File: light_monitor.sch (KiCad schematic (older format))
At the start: 28 parts, among them IC1 TSL237S-LF, J1 Conn_01x03, J2 Conn_01x04_Male, U1 STM32L432KCUx, U2 STDC14, U3 TG-3541CE, U4 sm_tsl237, U5 REG710-3, U6 LT1677CS8

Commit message: rev 10 board
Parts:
- removed H2: MountingHole, MountingHole:MountingHole_2.2mm_M2_Pad_Via, symbol Mechanical:MountingHole
- removed U4: sm_tsl237, bhimebau_lightsensor:tsl237t, symbol bhimebau_lightsensor:sm_tsl237
- removed U5: REG710-3, Package_TO_SOT_SMD:SOT-23-6_Handsoldering, symbol bhimebau-switch-mode-supply:REG710-3
- removed U6: LT1677CS8, ltc1677:SO-8_S, symbol ltc1677:LT1677CS8
- added C4, C6, C7: 0.1uF, Capacitor_SMD:C_0603_1608Metric_Pad1.05x0.95mm_HandSolder, symbol Device:C
- added C5: 1uF, Capacitor_SMD:C_0603_1608Metric_Pad1.05x0.95mm_HandSolder, symbol Device:C
- added R1, R10, R11, R12, R9: R_US, Resistor_SMD:R_0603_1608Metric_Pad1.05x0.95mm_HandSolder, symbol Device:R_US
- added TP1, TP10, TP11, TP2, TP3, TP4, TP5, TP6, TP7, TP8, TP9: TestPoint, TestPoint:TestPoint_Pad_D1.5mm, symbol Connector:TestPoint
- added U4: TPS7A05, Package_TO_SOT_SMD:SOT-23, symbol bhimebau_regulator:TPS7A05
- added U5: TPS22917, Package_TO_SOT_SMD:SOT-23-6_Handsoldering, symbol bhimebau_switch:TPS22917
- added U6: AD8515, Package_TO_SOT_SMD:SOT-353_SC-70-5_Handsoldering, symbol bhimebau_opamp:AD8515
- BT1: footprint bhimebau_battery:BR2330A_Horizontal_Circular_Holes -> bhimebau_battery:TLH-5935
- C1, C2: value 2.2uF -> 1uF
- C3: value 0.1uF -> 1uF
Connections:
- net labels added: +BATT, +VSW, CLKOUT, batt_measure, sensor_pwr
- net labels removed: current_feedback, sensor_3v, tsl237_pwr
- wire segments 100 -> 145
- no-connect marks 23 -> 18
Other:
- note added: "VDD = 2V"
- moved on the sheet: BT1, C11, D2, H1, H3, H4, IC1, R2

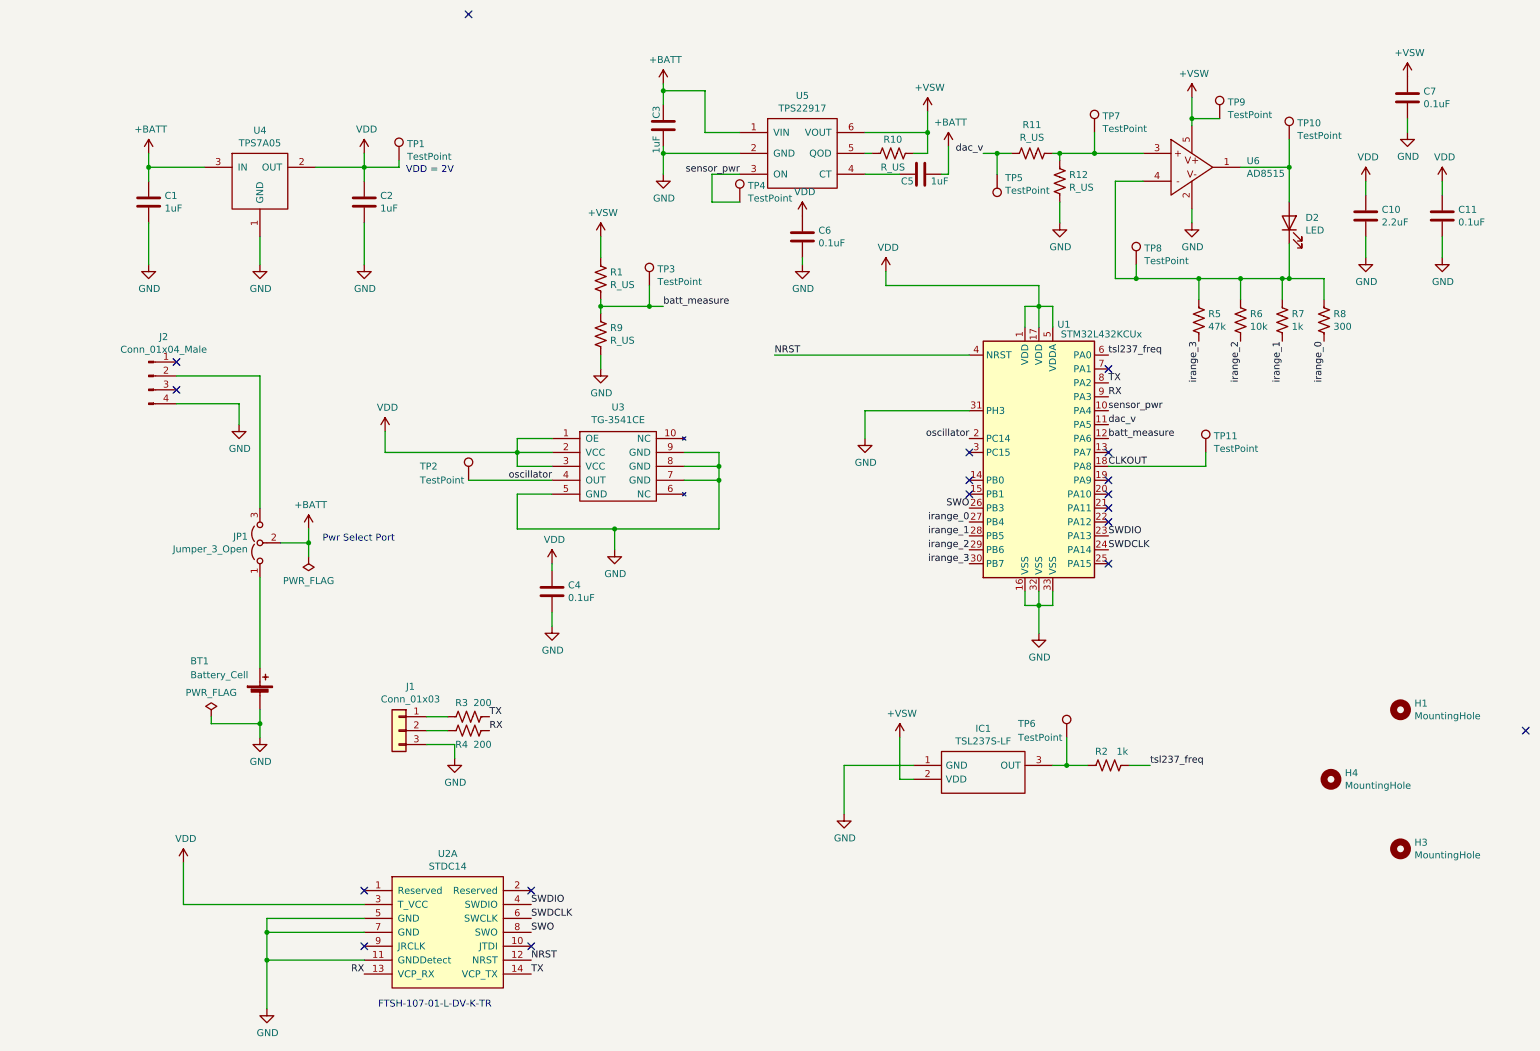
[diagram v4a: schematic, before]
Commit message: added the version used by the students
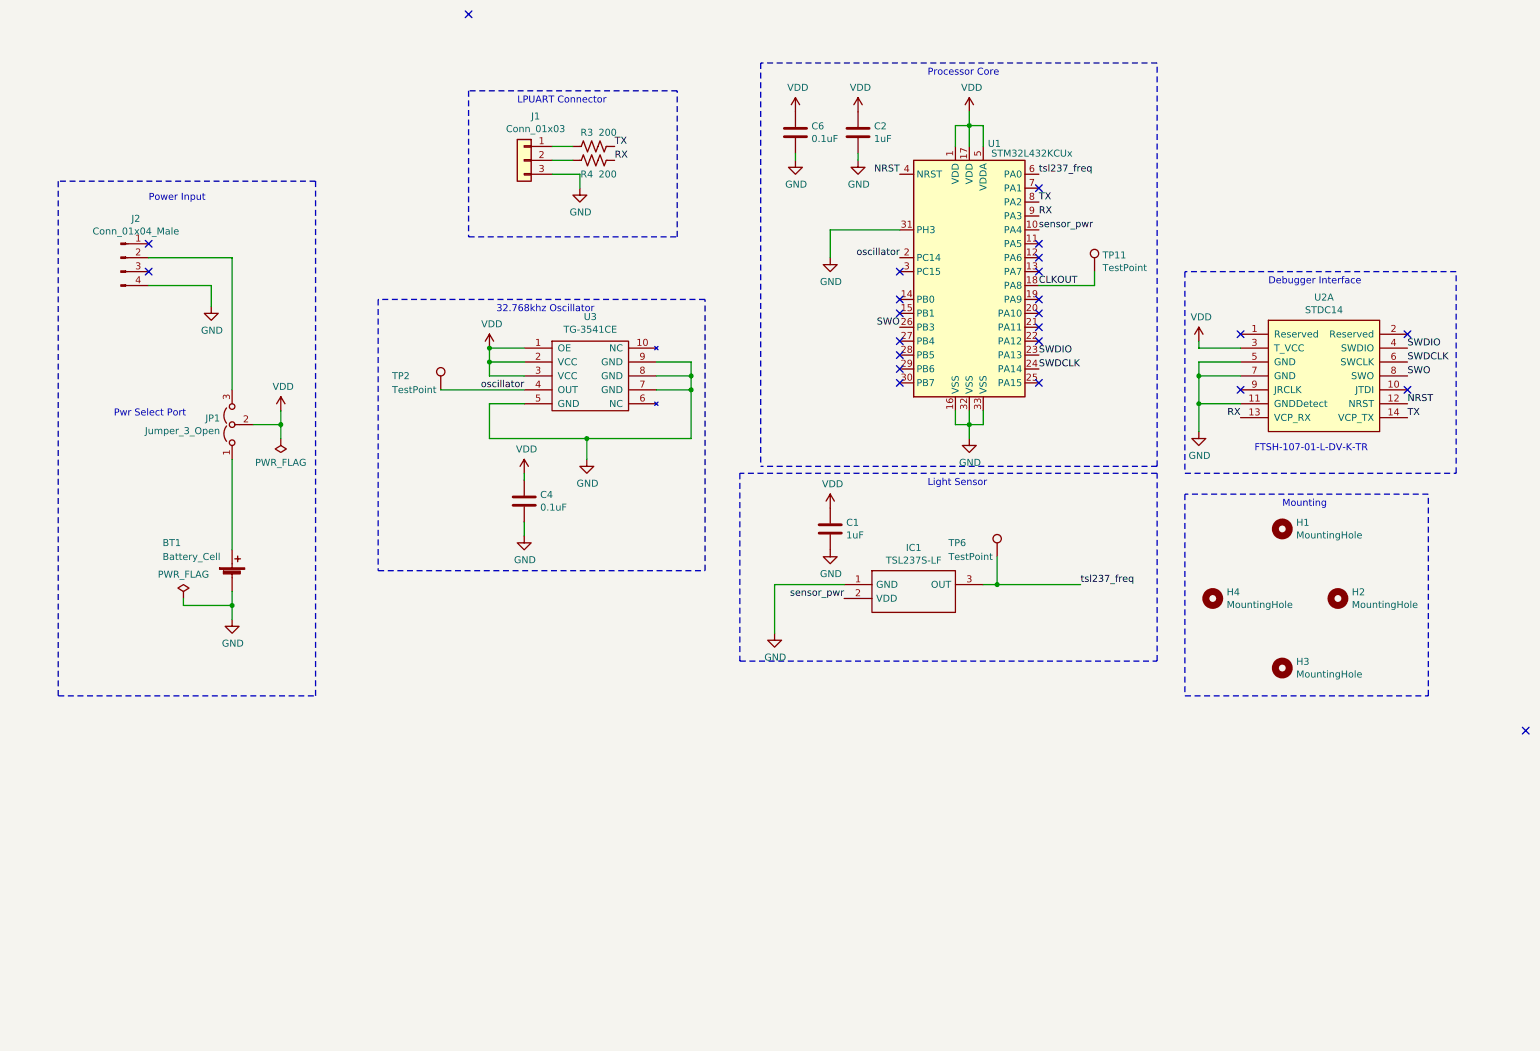
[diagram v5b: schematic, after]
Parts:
- removed C10: 2.2uF, Capacitor_SMD:C_0603_1608Metric_Pad1.05x0.95mm_HandSolder, symbol Device:C
- removed C11, C7: 0.1uF, Capacitor_SMD:C_0603_1608Metric_Pad1.05x0.95mm_HandSolder, symbol Device:C
- removed C3, C5: 1uF, Capacitor_SMD:C_0603_1608Metric_Pad1.05x0.95mm_HandSolder, symbol Device:C
- removed D2: LED, LED_SMD:LED_0603_1608Metric_Pad1.05x0.95mm_HandSolder, symbol Device:LED
- removed R1, R10, R11, R12, R9: R_US, Resistor_SMD:R_0603_1608Metric_Pad1.05x0.95mm_HandSolder, symbol Device:R_US
- removed R2, R7: 1k, Resistor_SMD:R_0603_1608Metric_Pad1.05x0.95mm_HandSolder, symbol Device:R_US
- removed R5: 47k, Resistor_SMD:R_0603_1608Metric_Pad1.05x0.95mm_HandSolder, symbol Device:R_US
- removed R6: 10k, Resistor_SMD:R_0603_1608Metric_Pad1.05x0.95mm_HandSolder, symbol Device:R_US
- removed R8: 300, Resistor_SMD:R_0603_1608Metric_Pad1.05x0.95mm_HandSolder, symbol Device:R_US
- removed TP1, TP10, TP3, TP4, TP5, TP7, TP8, TP9: TestPoint, TestPoint:TestPoint_Pad_D1.5mm, symbol Connector:TestPoint
- removed U4: TPS7A05, Package_TO_SOT_SMD:SOT-23, symbol bhimebau_regulator:TPS7A05
- removed U5: TPS22917, Package_TO_SOT_SMD:SOT-23-6_Handsoldering, symbol bhimebau_switch:TPS22917
- removed U6: AD8515, Package_TO_SOT_SMD:SOT-353_SC-70-5_Handsoldering, symbol bhimebau_opamp:AD8515
- added H2: MountingHole, MountingHole:MountingHole_2.2mm_M2_Pad_Via, symbol Mechanical:MountingHole
- BT1: footprint bhimebau_battery:TLH-5935 -> Battery:BatteryHolder_Keystone_1060_1x2032
- IC1: footprint SamacSys_Parts_3:TSL237S-LF -> e314-2020:TSL237S-LF
- U1: footprint Housings_DFN_QFN:QFN-32-1EP_5x5mm_Pitch0.5mm -> Package_DFN_QFN:QFN-32-1EP_5x5mm_P0.5mm_EP3.45x3.45mm
- U2: footprint bhimebau_inductor:ftsh_14p_connector -> e314-2020:ftsh_14p_connector
- U3: footprint bhimebau_oscillator:TG-3541CE -> e314-2020:TG-3541CE
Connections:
- net +BATT is gone; now on net VDD: C1.1, JP1.2 (C)
- net +VSW is gone; now on net sensor_pwr: IC1.2 (VDD)
- net tsl237_freq: now also IC1.3 (OUT), TP6.1
- net batt_measure: no longer names the net of U1.12 (PA6)
- net dac_v: no longer names the net of U1.11 (PA5)
- net irange_0: no longer names the net of U1.27 (PB4)
- net irange_1: no longer names the net of U1.28 (PB5)
- net irange_2: no longer names the net of U1.29 (PB6)
- net irange_3: no longer names the net of U1.30 (PB7)
- no-connect marks 18 -> 24
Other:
- note added: "32.768khz Oscillator \n"
- note added: "Debugger Interface"
- note added: "LPUART Connector"
- note added: "Light Sensor\n"
- note added: "Mounting\n"
- note added: "Power Input"
- note added: "Processor Core"
- note removed: "VDD = 2V"
- moved on the sheet: BT1, C4, C6, H1, H3, H4, IC1, J1, J2, JP1, R3, R4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

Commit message: checkpoint
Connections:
- net VDD: no longer C1.1
- net sensor_pwr: now also C1.1
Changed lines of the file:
@@
-$EndComp
-$Comp
-L power:VDD #PWR01
-U 1 1 5E6364B9
-P 6400 3800
-F 0 "#PWR01" H 6400 3650 50  0001 C CNN
-F 1 "VDD" H 6417 3973 50  0000 C CNN
-F 2 "" H 6400 3800 50  0001 C CNN
-F 3 "" H 6400 3800 50  0001 C CNN
-	1    6400 3800
-	1    0    0    -1
 $EndComp
 $Comp
@@
 Text Notes 4150 900  0    50   ~ 0
 LPUART Connector
+Text Label 6250 3700 2    50   ~ 0
+sensor_pwr
+Wire Wire Line
+	6250 3700 6400 3700
+Wire Wire Line
+	6400 3700 6400 3800
 $EndSCHEMATC
